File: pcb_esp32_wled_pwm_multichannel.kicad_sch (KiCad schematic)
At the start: 93 parts, among them J101 WJ2EDGRC-5.08-4P, J102 WJ2EDGRC-5.08-4P, J103 WJ2EDGRC-5.08-4P, J104 WJ2EDGRC-5.08-4P, J105 Conn_01x05_Male, J106 Conn_01x03_Female, J107 Conn_01x03_Female, J108 Conn_01x02_Female, J109 USB_C_Receptacle_USB2.0, Q101 IRLR8743TRPBF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

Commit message: change footprint of polarized C to larger version that actually exists. Update BOM
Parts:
- removed C106: 470uF/20V, Capacitor_SMD:CP_Elec_8x11.9, symbol Device:C_Polarized
- C116: footprint Capacitor_SMD:CP_Elec_5x5.4 -> Capacitor_SMD:CP_Elec_6.3x7.7; Distributor (none) -> LCSC; LCSC (none) -> C311622; MF (none) -> Lelon; MP (none) -> VZT101M1HTR-0607
- C117: footprint Capacitor_SMD:CP_Elec_5x5.4 -> Capacitor_SMD:CP_Elec_6.3x7.7; Distributor (none) -> LCSC; LCSC (none) -> C74623; MF (none) -> RVT0J331M0607; MP (none) -> ROQANG
- D118: SMD (none) -> 0
- J106, J107: Distributor (none) -> LCSC; LCSC (none) -> C49257; MF (none) -> generic; MP (none) -> PinHeader,P=2.54mm,3Pin,1Row,1A
- J108, L101, Q101, Q102, Q103, Q104, Q105, Q106, Q107, Q108, Q109, Q110, Q111, Q112: Distributor (none) -> LCSC
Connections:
- net RXD renamed RXcp21
- net RXD0 renamed RXDesp

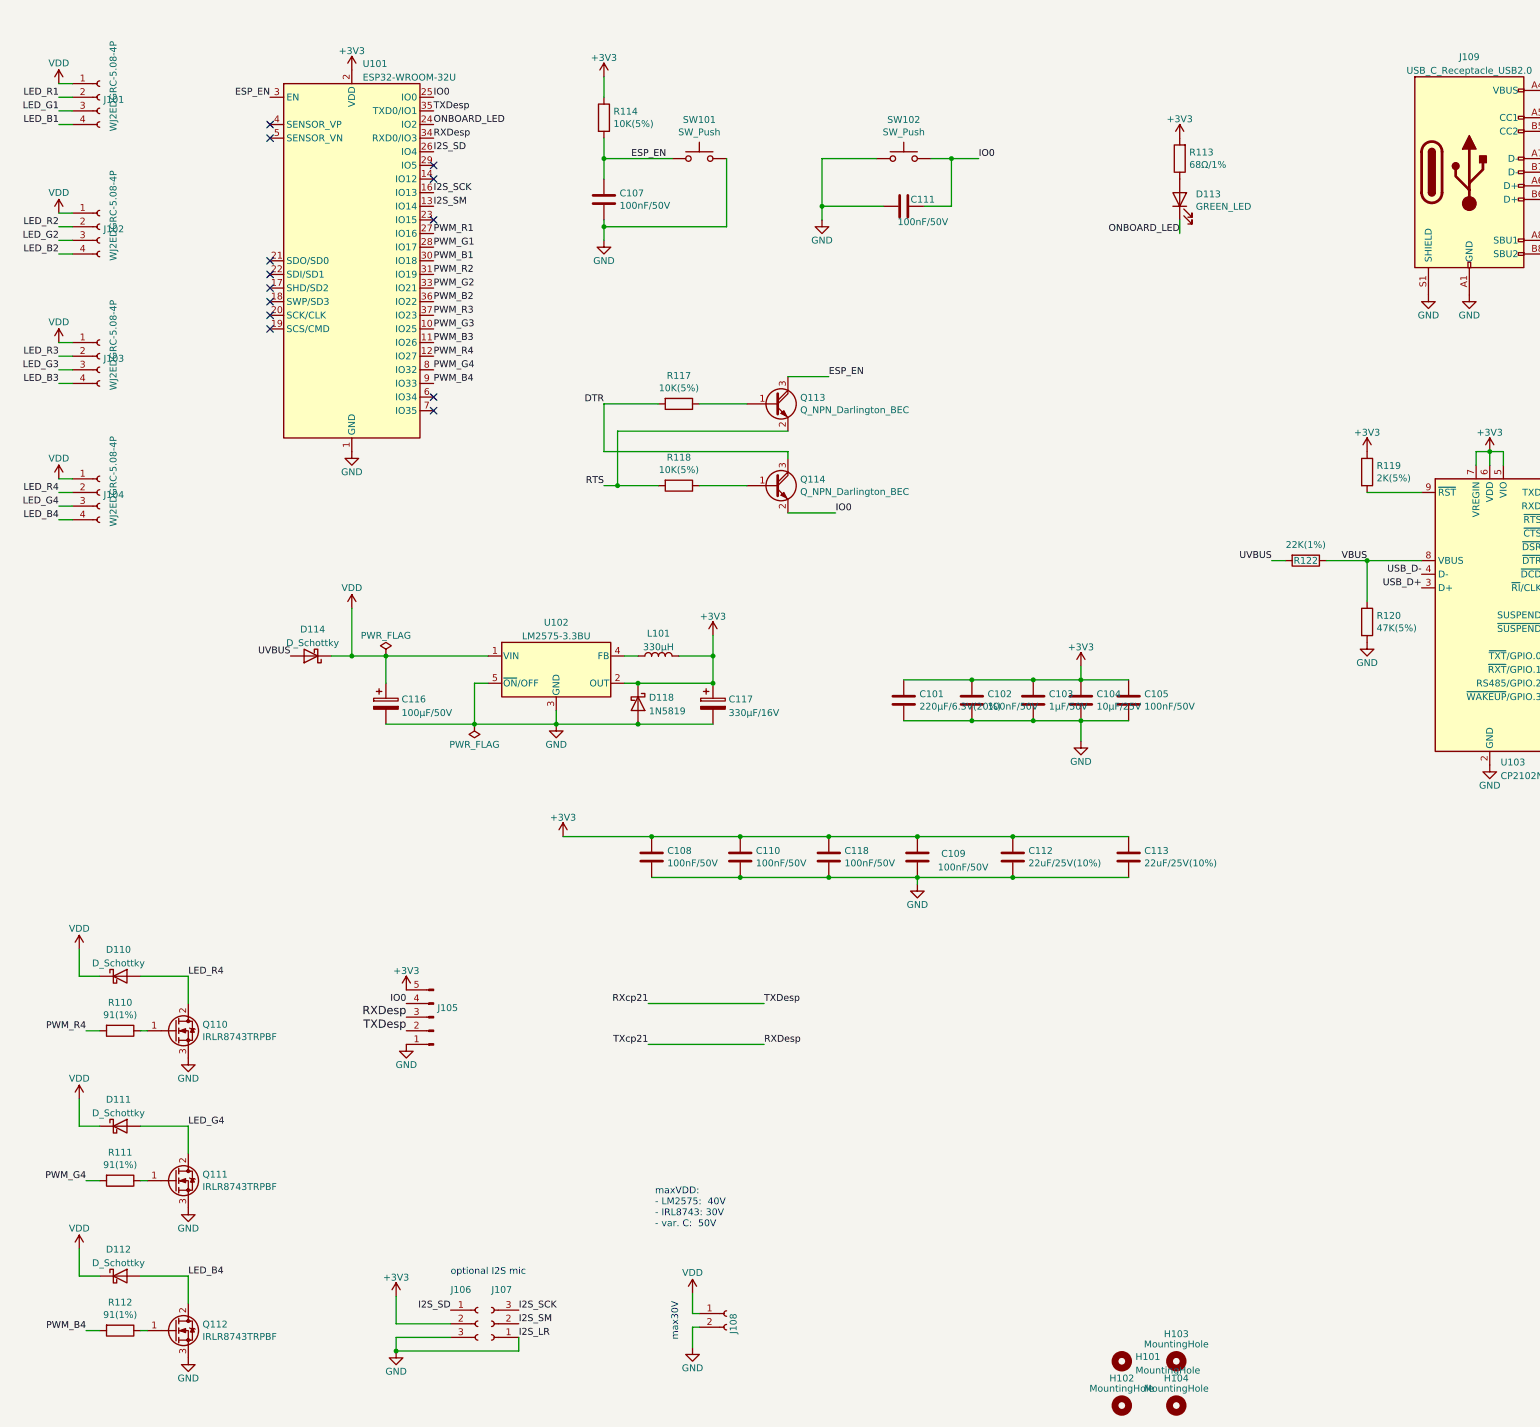
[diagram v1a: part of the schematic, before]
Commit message: fix description of C117
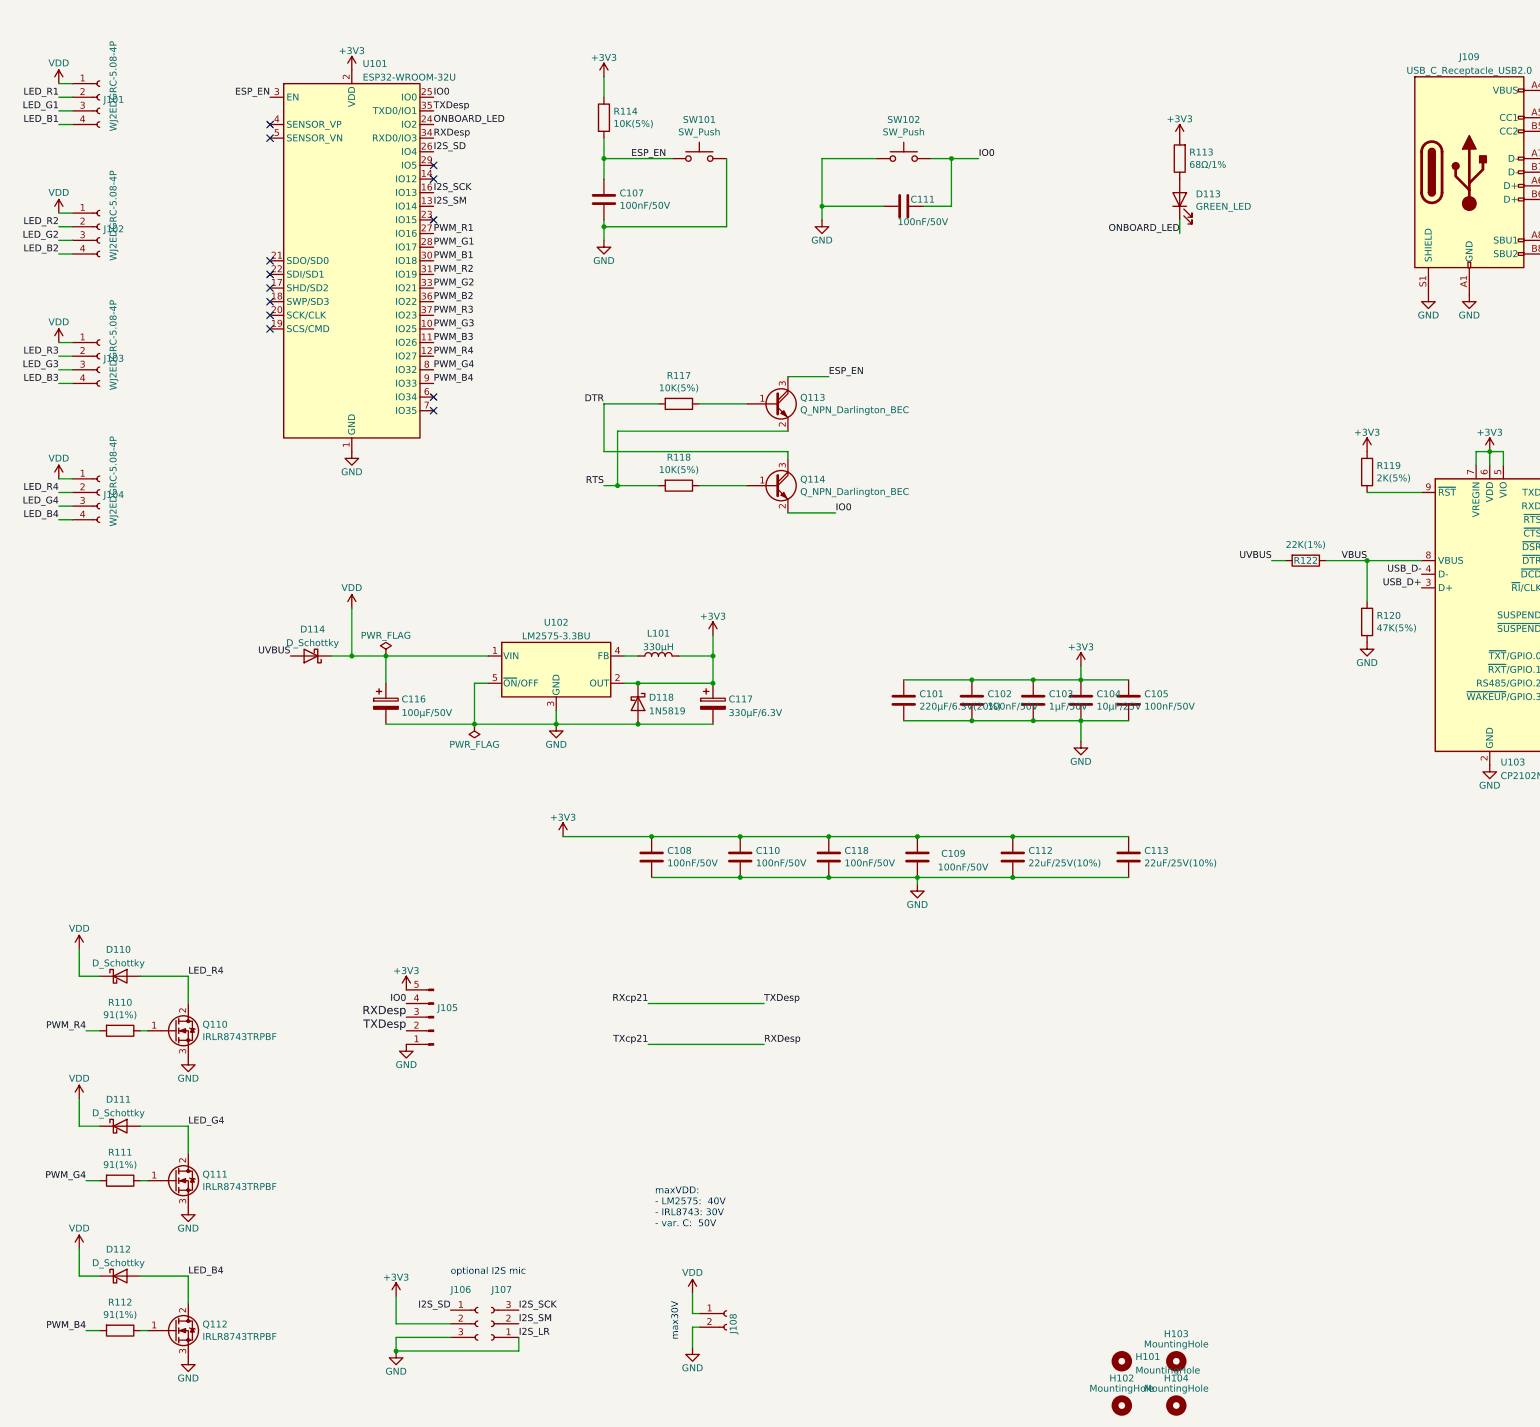
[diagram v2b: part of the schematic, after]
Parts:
- C117: value 330µF/16V -> 330µF/6.3V

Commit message: fix I2S microphone pin header. V3
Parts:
- J106, J107: LCSC C49257 -> C358717; MP PinHeader,P=2.54mm,3Pin,1Row,1A -> PinHeader,Feamle,P=2.54mm,3Pin,1Row,1A
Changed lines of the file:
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@@
       (effects (font (size 1.27 1.27)) hide)
     )
-    (property "MP" "PinHeader,P=2.54mm,3Pin,1Row,1A" (at 151.765 256.54 0)
+    (property "MP" "PinHeader,Feamle,P=2.54mm,3Pin,1Row,1A" (at 151.765 256.54 0)
       (effects (font (size 1.27 1.27)) hide)
     )
-    (property "LCSC" "C49257" (at 151.765 256.54 0)
+    (property "LCSC" "C358717" (at 151.765 256.54 0)
       (effects (font (size 1.27 1.27)) hide)
     )
@@
       (effects (font (size 1.27 1.27)) hide)
     )
-    (property "LCSC" "C49257" (at 154.305 256.54 0)
+    (property "LCSC" "C358717" (at 154.305 256.54 0)
       (effects (font (size 1.27 1.27)) hide)
     )
@@
       (effects (font (size 1.27 1.27)) hide)
     )
-    (property "MP" "PinHeader,P=2.54mm,3Pin,1Row,1A" (at 154.305 256.54 0)
+    (property "MP" "PinHeader,Feamle,P=2.54mm,3Pin,1Row,1A" (at 154.305 256.54 0)
       (effects (font (size 1.27 1.27)) hide)
     )

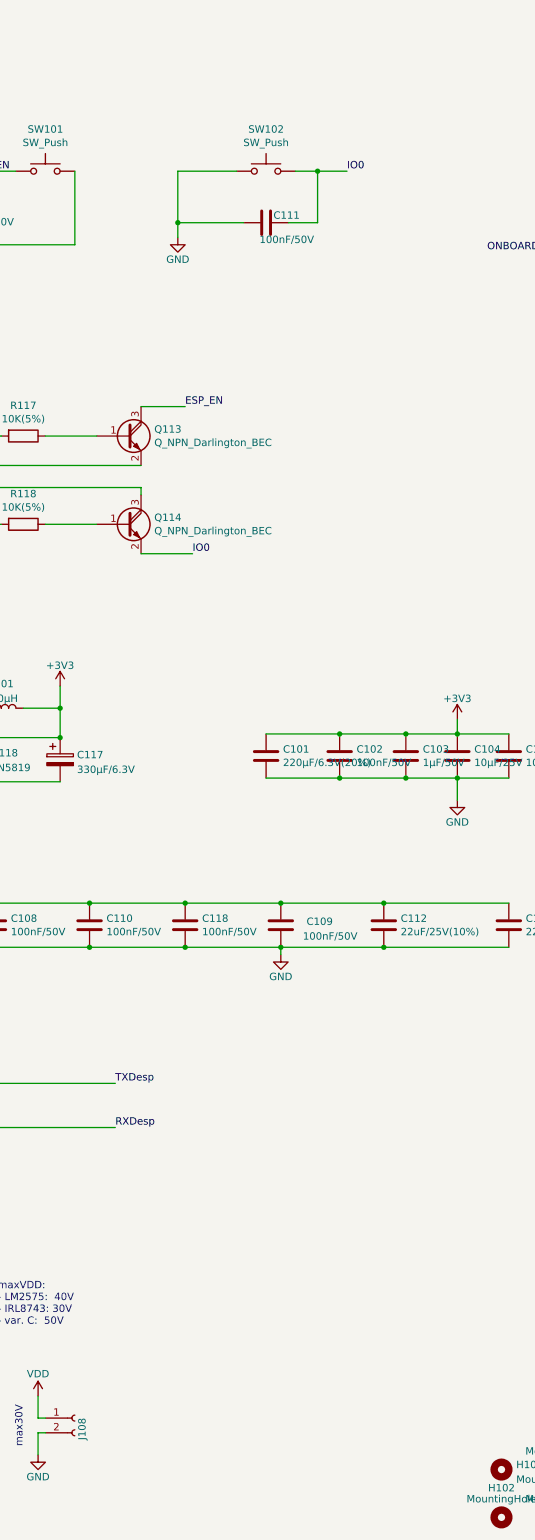
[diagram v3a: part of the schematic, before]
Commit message: update future v3: reduce capacity of C111 debouncing BOOT0/IO0, so we are less likely to enter bootloader-mode on power-up
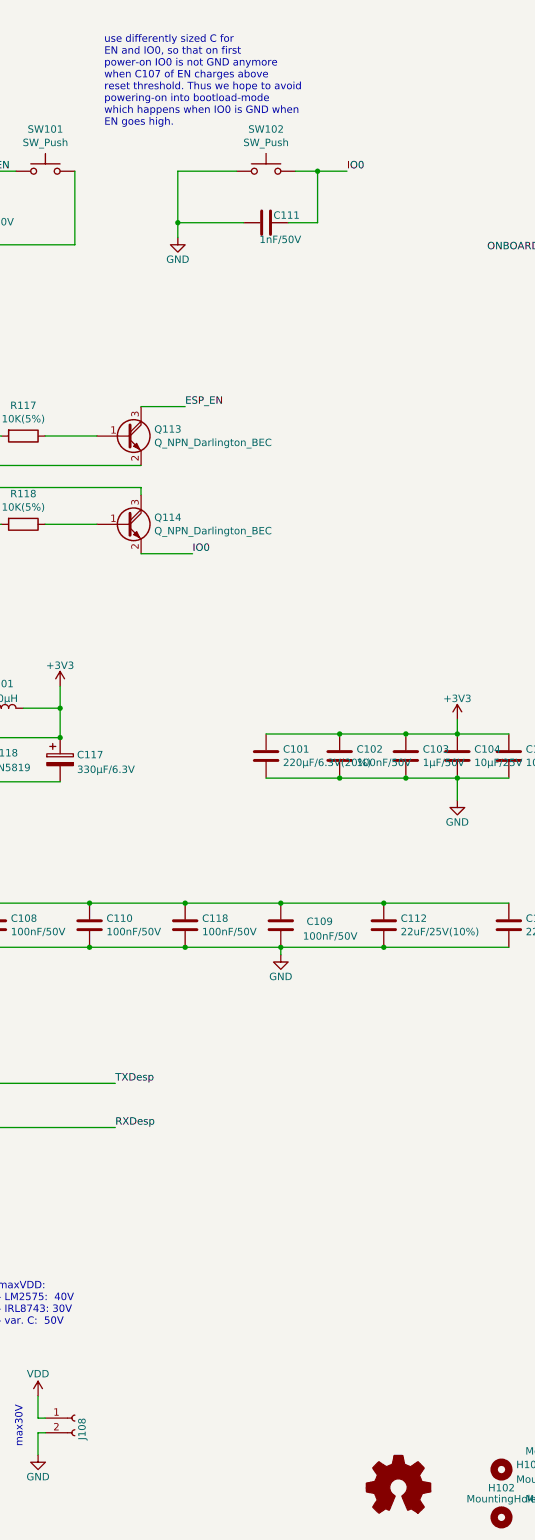
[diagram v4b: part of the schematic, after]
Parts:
- added SYM101: Logo_Open_Hardware_Small, Symbol:OSHW-Logo2_7.3x6mm_SilkScreen, symbol Graphic:Logo_Open_Hardware_Small
- C111: value 100nF/50V -> 1nF/50V; LCSC C42998 -> C100040; MF FH -> YAGEO; MP 0603F104M500NT -> CC0603KRX7R9BB102
- H101, H102, H103, H104: now left out of the parts list
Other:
- note added: "use differently sized C for EN and IO0, so that on first power-on IO0 is not GND anymore when C107 of EN charges above reset threshold. Thus we hope to avoid powering-on into bootload-mode which happens when IO0 is GND when EN goes high."

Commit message: several fixes, thanks to mickdermack for reviewing
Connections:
- net +3V3: now also U102.4 (FB); no longer D118.1 (K), U102.2 (OUT)
- net DTR: now also Q114.2 (E); no longer Q114.3 (C)
- net IO0: now also Q114.3 (C); no longer Q114.2 (E)
- net at L101.1: now also D118.1 (K), U102.2 (OUT); no longer U102.4 (FB)
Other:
- note added: "C for CP2102N"
- note added: "C for ESP"
- moved on the sheet: C101, C102, C103, C104, C105, C116, C117, D114, D118, L101, U102

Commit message: wip: re-add 10ks discharge R to MosFETs
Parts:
- added R131, R132, R133, R134, R135, R136, R137, R138, R139, R140, R141, R142: 10K(5%), Resistor_SMD:R_0603_1608Metric, symbol Device:R
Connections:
- net GND: now also R131.2, R132.2, R133.2, R134.2, R135.2, R136.2, R137.2, R138.2, R139.2, R140.2, R141.2, R142.2
- net at Q108.1 (G), R108.1: now also R138.1
- net at Q107.1 (G), R107.1: now also R137.1
- net at Q101.1 (G), R101.1: now also R131.1
- net at Q111.1 (G), R111.1: now also R141.1
- net at Q110.1 (G), R110.1: now also R140.1
- net at Q103.1 (G), R103.1: now also R133.1
- net at Q112.1 (G), R112.1: now also R142.1
- net at Q104.1 (G), R104.1: now also R134.1
- net at Q105.1 (G), R105.1: now also R135.1
- net at Q102.1 (G), R102.1: now also R132.1
- net at Q106.1 (G), R106.1: now also R136.1
- net at Q109.1 (G), R109.1: now also R139.1
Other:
- moved on the sheet: C101, C102, C103, C104, C105, C107, C108, C109, C110, C111, C112, C113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
